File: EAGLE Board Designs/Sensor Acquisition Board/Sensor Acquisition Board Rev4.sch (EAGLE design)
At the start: 22 parts, among them J1 CONNECTOR-SENSOR_NF_S_RA_BLACK, J10 CONNECTOR-SENSOR_NF_S_RA_BLACK, J2 CONNECTOR-CAN_NF_S_RA_BLACK, J3 JUMPER_1X02_, J4 CONNECTOR-SENSOR_NF_S_RA_BLACK, J5 CONNECTOR-SENSOR_NF_S_RA_BLACK, J6 CONNECTOR-SENSOR_NF_S_RA_BLACK, J7 CONNECTOR-SENSOR_NF_S_RA_BLACK, J8 CONNECTOR-SENSOR_NF_S_RA_BLACK, J9 CONNECTOR-SENSOR_NF_S_RA_BLACK, U1 VOLTAGE_REGULATOR_SOT223_5V, U3 TCAN1051HQV-Q1

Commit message: Created Sensor Acquisition Board rev4 board
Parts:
- J10: value CONNECTOR-SENSOR_NF_S_RA_BLACK -> JUMPER_1X02_; device HyTechDevices:CONNECTOR-SENSOR_NF_S_RA_BLACK -> HyTechDevices:JUMPER_1X02_
- J2: value CONNECTOR-CAN_NF_S_RA_BLACK -> CONNECTOR-SENSOR_NF_S_RA_BLACK; device HyTechDevices:CONNECTOR-CAN_NF_S_RA_BLACK -> HyTechDevices:CONNECTOR-SENSOR_NF_S_RA_BLACK
- J3: value JUMPER_1X02_ -> CONNECTOR-SENSOR_NF_S_RA_BLACK; device HyTechDevices:JUMPER_1X02_ -> HyTechDevices:CONNECTOR-SENSOR_NF_S_RA_BLACK
- J9: value CONNECTOR-SENSOR_NF_S_RA_BLACK -> CONNECTOR-CAN_NF_S_RA_BLACK; device HyTechDevices:CONNECTOR-SENSOR_NF_S_RA_BLACK -> HyTechDevices:CONNECTOR-CAN_NF_S_RA_BLACK
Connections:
- net +12V: now also J9.+12V; no longer J2.+12V
- net +5V: now also J2.VDD, J3.VDD; no longer J10.VDD, J9.VDD
- net CANH: now also J10.P$1, J9.CANH; no longer J2.CANH, J3.P$1
- net CANL: now also J10.P$2, J9.CANL; no longer J2.CANL, J3.P$2
- net GND: now also J3.GND; no longer J10.GND
- net SENSOR_2: now also J2.CH1, J2.CH2; no longer J5.CH1, J5.CH2
- net SENSOR_3: now also J3.CH1, J3.CH2; no longer J6.CH1, J6.CH2
- net SENSOR_4: now also J4.CH1, J4.CH2; no longer J10.CH1, J10.CH2
- net SENSOR_5: now also J5.CH1, J5.CH2; no longer J7.CH1, J7.CH2
- net SENSOR_6: now also J6.CH1, J6.CH2; no longer J4.CH1, J4.CH2
- net SENSOR_7: now also J7.CH1, J7.CH2; no longer J8.CH1, J8.CH2
- net SENSOR_8: now also J8.CH1, J8.CH2; no longer J9.CH1, J9.CH2
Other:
- moved on the sheet: J2, J4, J5, J6, J7, J8, J9

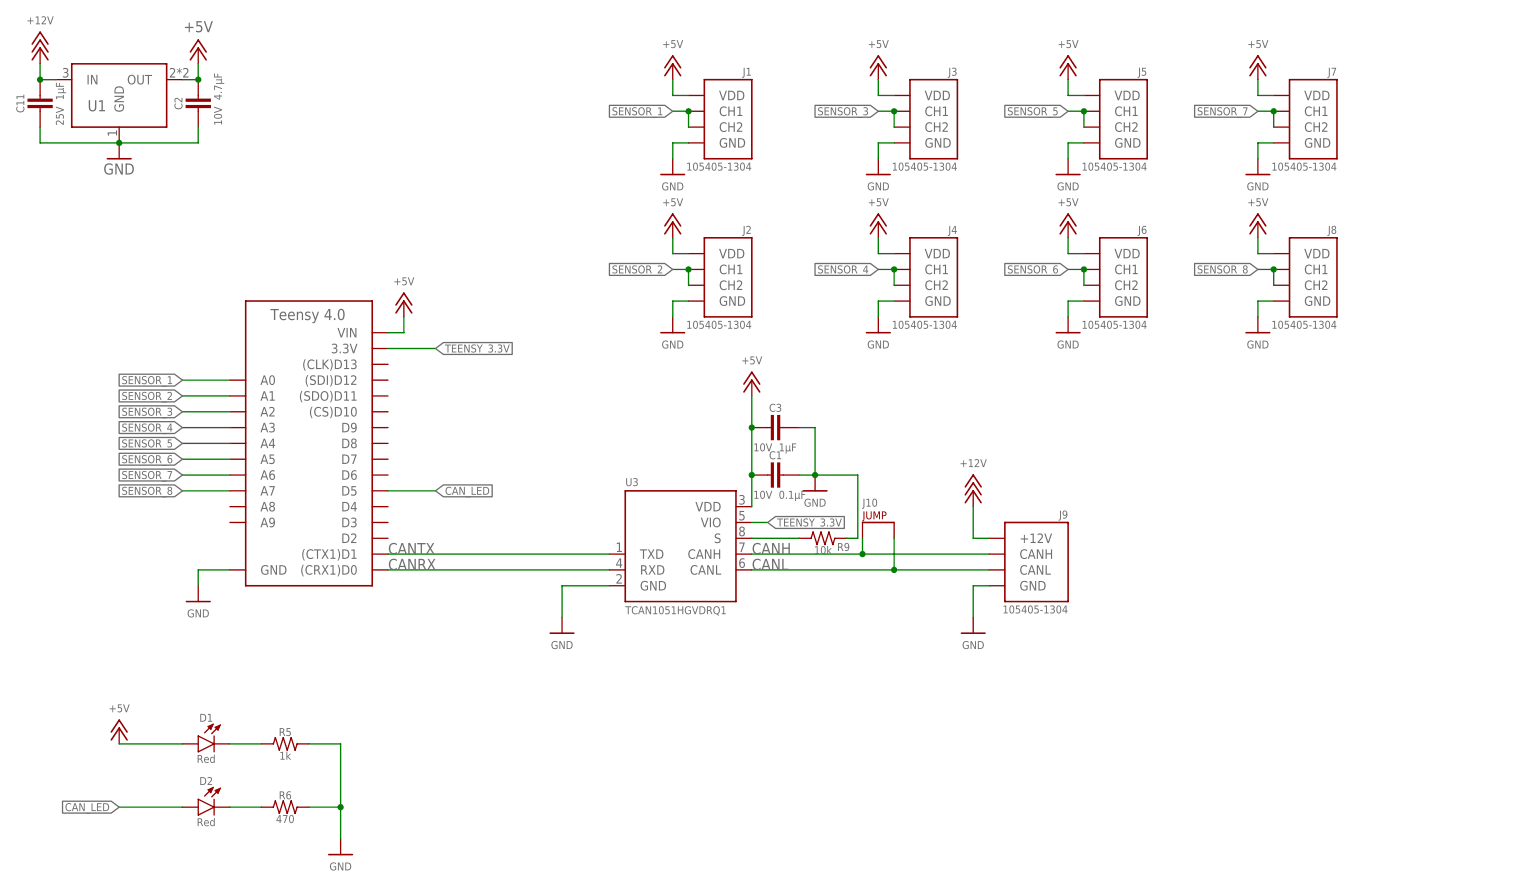
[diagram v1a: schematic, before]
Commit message: SAB rev4 voltage divider changes (not final)
Resistance values may be incorrect, but the part is there for now.
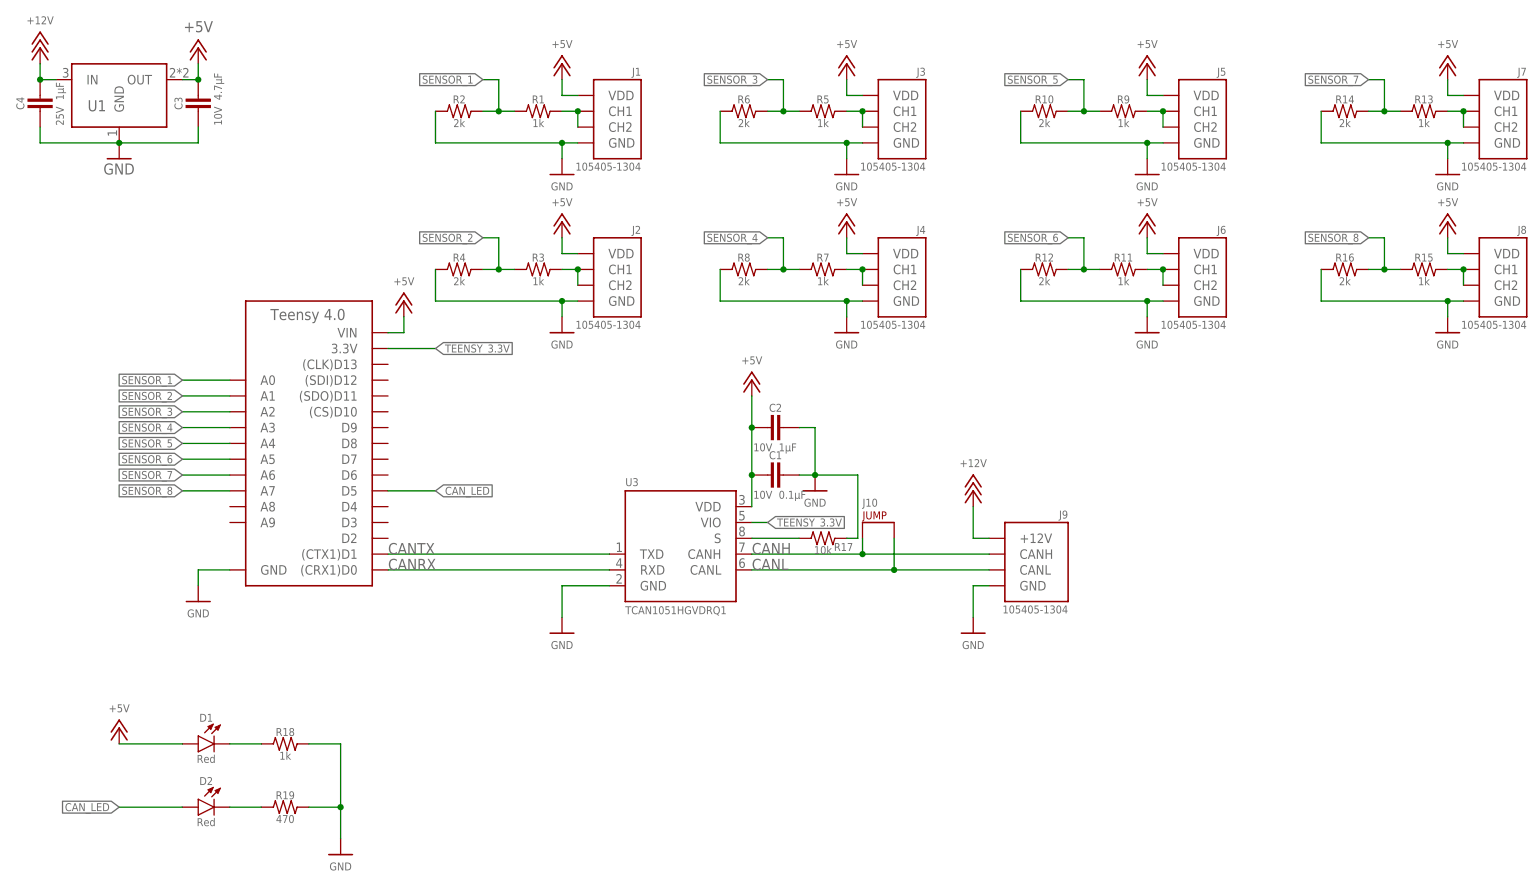
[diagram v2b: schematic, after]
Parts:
- added R1, R11, R13, R15, R18, R3, R7: RESISTOR_0603_1K, HyTechDevices:RESISTOR_0603_1K
- added R10, R12, R14, R16, R2, R4, R8: RESISTOR_0603_2K, HyTechDevices:RESISTOR_0603_2K
- added R17: RESISTOR_0603_10K, HyTechDevices:RESISTOR_0603_10K
- added R19: RESISTOR_0603_470, HyTechDevices:RESISTOR_0603_470
- C2: value CAPACITOR_0603_10V_4.7UF -> CAPACITOR_0603_10V_1UF; device HyTechDevices:CAPACITOR_0603_10V_4.7UF -> HyTechDevices:CAPACITOR_0603_10V_1UF
- C3: value CAPACITOR_0603_10V_1UF -> CAPACITOR_0603_10V_4.7UF; device HyTechDevices:CAPACITOR_0603_10V_1UF -> HyTechDevices:CAPACITOR_0603_10V_4.7UF
- R6: value RESISTOR_0603_470 -> RESISTOR_0603_2K; device HyTechDevices:RESISTOR_0603_470 -> HyTechDevices:RESISTOR_0603_2K
- R9: value RESISTOR_0603_10K -> RESISTOR_0603_1K; device HyTechDevices:RESISTOR_0603_10K -> HyTechDevices:RESISTOR_0603_1K
- renumbered C11 to C4
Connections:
- new net N$10: J2.CH1, J2.CH2, R3.2
- new net N$11: J3.CH1, J3.CH2, R5.2
- new net N$3: J8.CH1, J8.CH2, R15.2
- new net N$5: J7.CH1, J7.CH2, R13.2
- new net N$6: J5.CH1, J5.CH2, R9.2
- new net N$7: J6.CH1, J6.CH2, R11.2
- new net N$8: J1.CH1, J1.CH2, R1.2
- new net N$9: J4.CH1, J4.CH2, R7.2
- net +5V: now also C2.2, C3.1; no longer C2.1, C3.2
- net GND: now also C2.1, C3.2, R10.1, R12.1, R14.1, R16.1, R17.2, R18.2, R19.2, R2.1, R4.1, R6.1, R8.1; no longer C2.2, C3.1, R5.2, R6.2, R9.2
- net N$1: now also R18.1; no longer R5.1
- net N$2: now also R19.1; no longer R6.1
- net N$4: now also R17.1; no longer R9.1
- net SENSOR_1: now also R1.1, R2.2; no longer J1.CH1, J1.CH2
- net SENSOR_2: now also R3.1, R4.2; no longer J2.CH1, J2.CH2
- net SENSOR_3: now also R5.1, R6.2; no longer J3.CH1, J3.CH2
- net SENSOR_4: now also R7.1, R8.2; no longer J4.CH1, J4.CH2
- net SENSOR_5: now also R10.2, R9.1; no longer J5.CH1, J5.CH2
- net SENSOR_6: now also R11.1, R12.2; no longer J6.CH1, J6.CH2
- net SENSOR_7: now also R13.1, R14.2; no longer J7.CH1, J7.CH2
- net SENSOR_8: now also R15.1, R16.2; no longer J8.CH1, J8.CH2
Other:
- moved on the sheet: C2, C3, J1, J2, J3, J4, J5, J6, J7, J8, R5, R6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

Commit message: Finished SAB Rev4
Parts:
- A1: value TEENSY_4.0 -> TEENSY_3.2; device HyTechDevices:TEENSY_4.0 -> HyTechDevices:TEENSY_3.2
- R1, R11, R13, R15, R3, R5, R7, R9: value RESISTOR_0603_1K -> RESISTOR_0603_10K; device HyTechDevices:RESISTOR_0603_1K -> HyTechDevices:RESISTOR_0603_10K
- R10, R12, R14, R16, R2, R4, R6, R8: value RESISTOR_0603_2K -> RESISTOR_0603_12K; device HyTechDevices:RESISTOR_0603_2K -> HyTechDevices:RESISTOR_0603_12K
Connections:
- removed net CANRX: A1.(CRX1)D0, U3.RXD
- removed net CANTX: A1.(CTX1)D1, U3.TXD
- new net CAN_RX: A1.(CRX)D4, U3.RXD
- new net CAN_TX: A1.(CTX)D3, U3.TXD
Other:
- moved on the sheet: C1, C2, J10, J9, R17, U3
